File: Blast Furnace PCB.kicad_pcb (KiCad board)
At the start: 2 copper layers, 84 x 60 mm, 35 parts, among them J1 Thermocouple_Screw_Terminal_0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, J2 9V_Conn_01x02, J3 Conn_02x06_Odd_Even, Q1 BSS138, Q2 BSS138, SW1 POWER_SWITCH, U1 MAX31856, U2 I2C_16x2_LCD

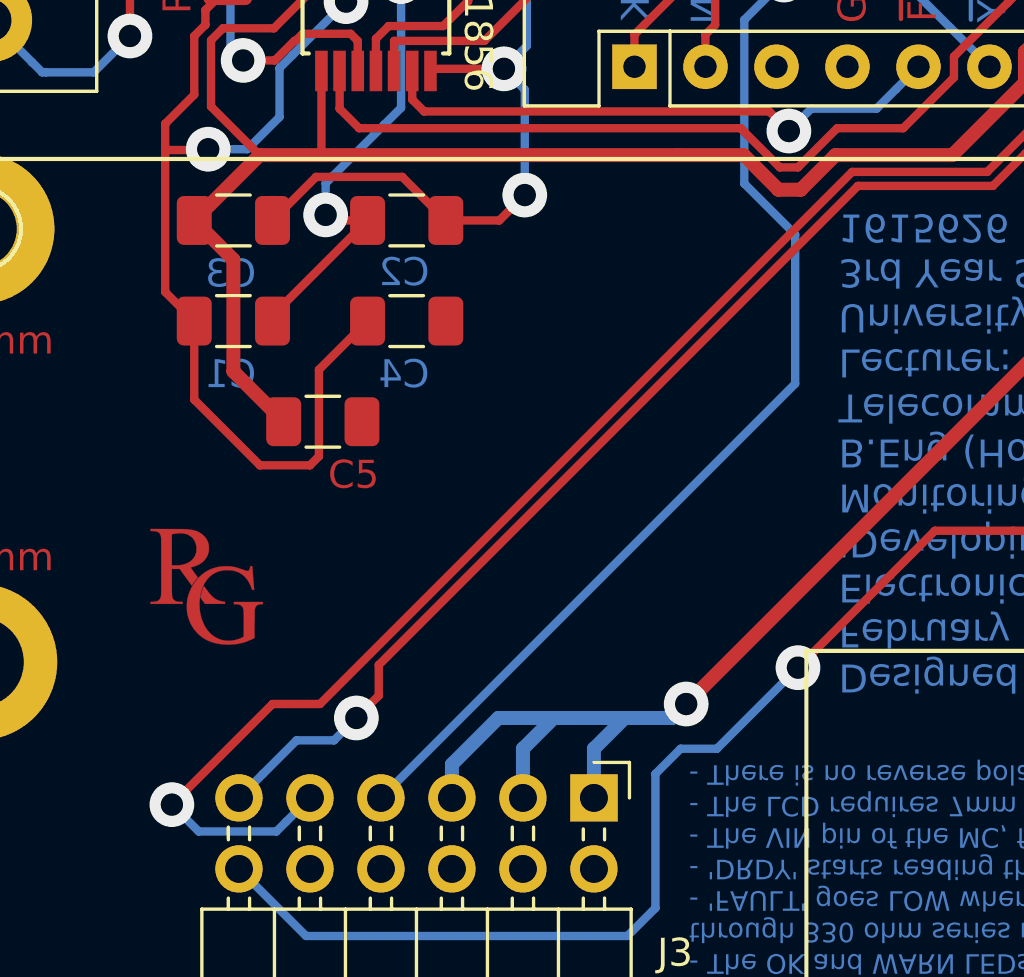
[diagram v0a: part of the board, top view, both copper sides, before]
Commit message: added silly test track
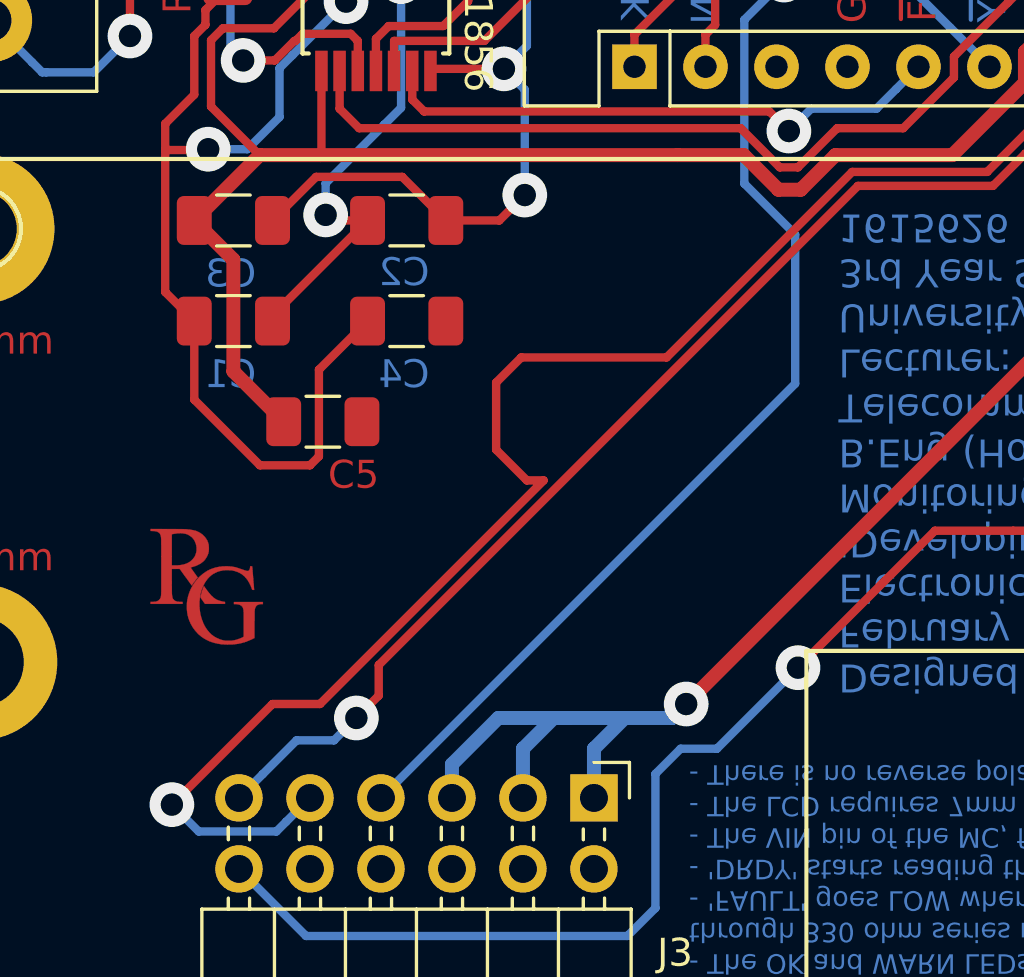
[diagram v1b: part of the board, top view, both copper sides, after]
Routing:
- net /D6: track 61.1 -> 65.9 mm
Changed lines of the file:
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@@
     (thickness 1.6)
     (drawings 81)
-    (tracks 426)
+    (tracks 431)
     (zones 0)
     (modules 35)
@@
   (segment (start 121.150001 111.649999) (end 122.151371 111.649999) (width 0.3) (layer B.Cu) (net 25))
   (segment (start 120.3 112.5) (end 121.150001 111.649999) (width 0.3) (layer B.Cu) (net 25))
-  (segment (start 122.050001 110.952001) (end 120.502002 112.5) (width 0.3) (layer F.Cu) (net 25))
-  (segment (start 122.050001 109.847999) (end 122.050001 110.952001) (width 0.3) (layer F.Cu) (net 25))
-  (segment (start 121.452001 109.249999) (end 122.050001 109.847999) (width 0.3) (layer F.Cu) (net 25))
-  (segment (start 119.482881 109.249999) (end 121.452001 109.249999) (width 0.3) (layer F.Cu) (net 25))
-  (segment (start 117.67067 111.06221) (end 119.482881 109.249999) (width 0.3) (layer F.Cu) (net 25))
-  (segment (start 120.502002 112.5) (end 120.3 112.5) (width 0.3) (layer F.Cu) (net 25))
-  (segment (start 112.83779 111.06221) (end 117.67067 111.06221) (width 0.3) (layer F.Cu) (net 25))
-  (segment (start 93.8 130.1) (end 112.83779 111.06221) (width 0.3) (layer F.Cu) (net 25))
-  (segment (start 93.2 130.1) (end 93.8 130.1) (width 0.3) (layer F.Cu) (net 25))
   (via (at 88.5 133.7) (size 1.6) (drill 0.8) (layers F.Cu B.Cu) (net 25))
-  (segment (start 93.2 130.1) (end 92.1 130.1) (width 0.3) (layer F.Cu) (net 25))
-  (segment (start 92.1 130.1) (end 88.5 133.7) (width 0.3) (layer F.Cu) (net 25))
   (segment (start 92.590001 134.309999) (end 93.44 133.46) (width 0.3) (layer B.Cu) (net 25))
   (segment (start 92.239999 134.660001) (end 92.590001 134.309999) (width 0.3) (layer B.Cu) (net 25))
@@
   (segment (start 88.5 133.7) (end 89.460001 134.660001) (width 0.3) (layer B.Cu) (net 25))
   (via (at 120.3 112.5) (size 1.6) (drill 0.8) (layers F.Cu B.Cu) (net 25))
+  (segment (start 122.050001 109.847999) (end 122.050001 110.952001) (width 0.3) (layer F.Cu) (net 25))
+  (segment (start 120.502002 112.5) (end 120.3 112.5) (width 0.3) (layer F.Cu) (net 25))
+  (segment (start 121.452001 109.249999) (end 122.050001 109.847999) (width 0.3) (layer F.Cu) (net 25))
+  (segment (start 119.482881 109.249999) (end 121.452001 109.249999) (width 0.3) (layer F.Cu) (net 25))
+  (segment (start 112.83779 111.06221) (end 117.67067 111.06221) (width 0.3) (layer F.Cu) (net 25))
+  (segment (start 101 117.7) (end 106.2 117.7) (width 0.3) (layer F.Cu) (net 25))
+  (segment (start 122.050001 110.952001) (end 120.502002 112.5) (width 0.3) (layer F.Cu) (net 25))
+  (segment (start 100.1 118.6) (end 101 117.7) (width 0.3) (layer F.Cu) (net 25))
+  (segment (start 106.2 117.7) (end 112.83779 111.06221) (width 0.3) (layer F.Cu) (net 25))
+  (segment (start 88.5 133.7) (end 92.1 130.1) (width 0.3) (layer F.Cu) (net 25))
+  (segment (start 117.67067 111.06221) (end 119.482881 109.249999) (width 0.3) (layer F.Cu) (net 25))
+  (segment (start 92.1 130.1) (end 93.8 130.1) (width 0.3) (layer F.Cu) (net 25))
+  (segment (start 93.8 130.1) (end 101.8 122.1) (width 0.3) (layer F.Cu) (net 25))
+  (segment (start 101.8 122.1) (end 101.2 122.1) (width 0.3) (layer F.Cu) (net 25))
+  (segment (start 101.2 122.1) (end 100.1 121) (width 0.3) (layer F.Cu) (net 25))
+  (segment (start 100.1 121) (end 100.1 118.6) (width 0.3) (layer F.Cu) (net 25))
   (zone (net 1) (net_name GND) (layer F.Cu) (hatch edge 0.508)
     (connect_pads (clearance 0.508))

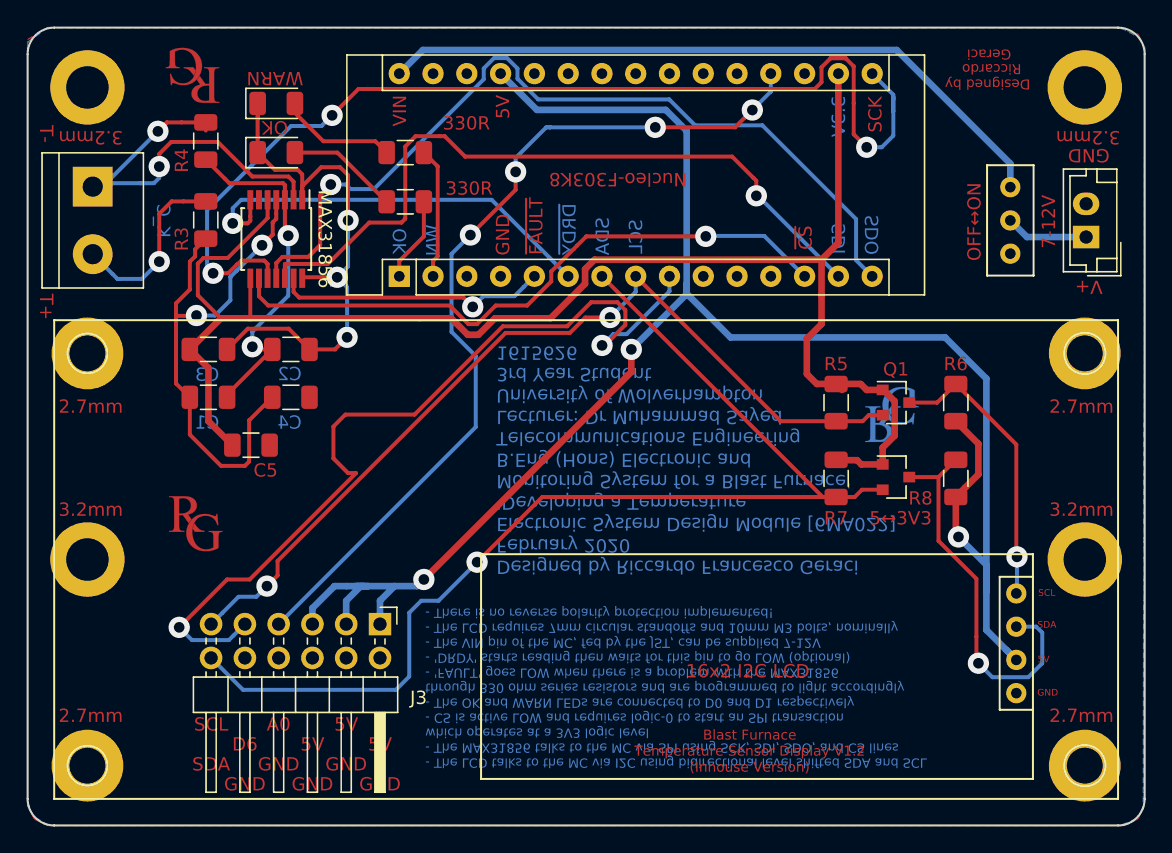
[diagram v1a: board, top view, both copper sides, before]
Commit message: Connected the missed nucleo pads that were meant to be backcopper as chris' email pointed out and made them all on backcopper as they should have been
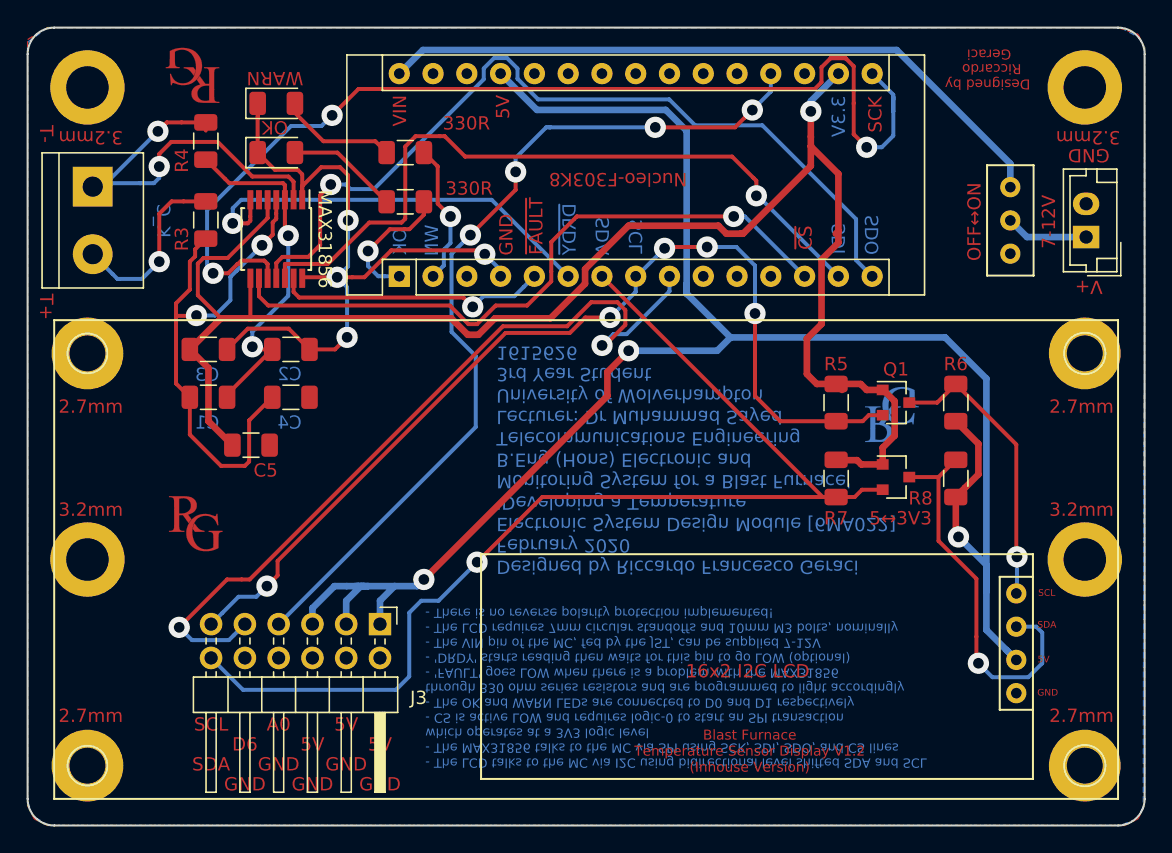
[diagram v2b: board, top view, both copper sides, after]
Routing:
- net GND: track 41.2 -> 55.4 mm, vias 3 -> 4
- net SCL_3V3: track 68.6 -> 76.1 mm, vias 2 -> 5
- net 3V3: track 116.8 -> 122.9 mm, vias 0 -> 1
- net /D6: track 65.9 -> 61.1 mm
- net Net-(A1-Pad1): track 6.37 -> 10.1 mm, vias 0 -> 1
- net /CS: track 47.7 -> 50.2 mm
- net 5V: track 140.7 -> 142.7 mm
- net Net-(A1-Pad2): track 9.87 -> 10.7 mm, vias 0 -> 1

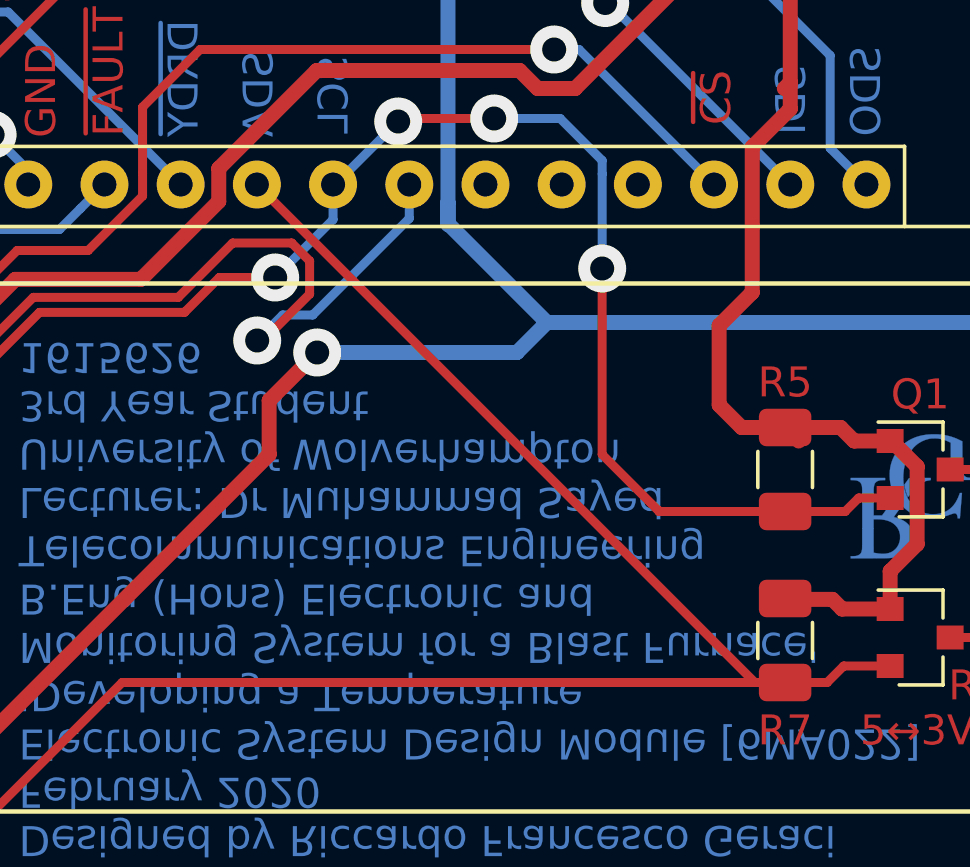
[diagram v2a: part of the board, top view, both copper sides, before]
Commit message: Created gerber files for V1.2.2, and sent to chris
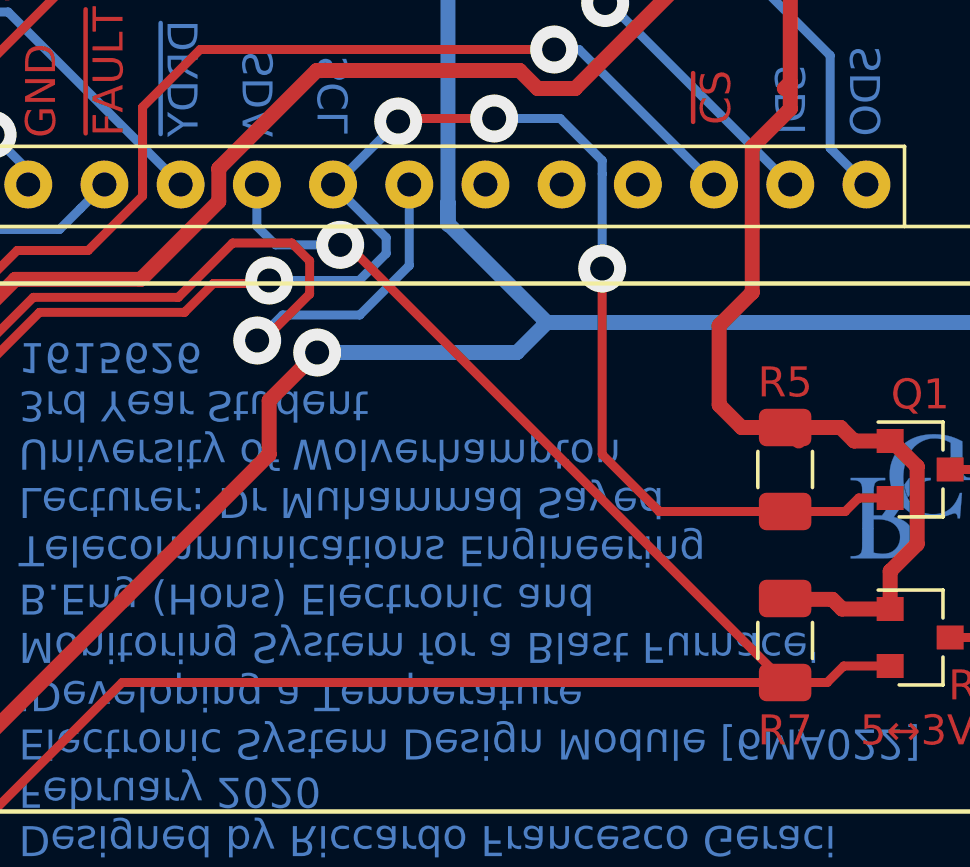
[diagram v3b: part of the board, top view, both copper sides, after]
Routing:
- net SCL_3V3: track 76.1 -> 79.3 mm
- net SDA_3V3: track 85.0 -> 86.8 mm, vias 1 -> 2
- net /D6: track 61.1 -> 62.1 mm
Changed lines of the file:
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@@
     (thickness 1.6)
     (drawings 81)
-    (tracks 469)
+    (tracks 477)
     (zones 0)
     (modules 35)
@@
       (drillshape 0)
       (scaleselection 1)
-      (outputdirectory "Gerber Files/V1.2.1 Chris Version, Back Copper Version/test/"))
+      (outputdirectory "Gerber Files/V1.2.2 Chris Version, ALL back copper!/"))
   )
   (net 0 "")
@@
   (segment (start 126.659999 96.359999) (end 125.09 94.79) (width 0.5) (layer B.Cu) (net 12))
   (segment (start 129.959999 111.9) (end 146.1 111.9) (width 0.5) (layer B.Cu) (net 12))
-  (segment (start 126.659999 108.6) (end 129.959999 111.9) (width 0.5) (layer B.Cu) (net 12))
   (segment (start 126.659999 107.9) (end 126.659999 108.6) (width 0.5) (layer B.Cu) (net 12))
   (segment (start 146.1 111.9) (end 149.2 115) (width 0.5) (layer B.Cu) (net 12))
@@
   (segment (start 128.959999 112.9) (end 129.959999 111.9) (width 0.5) (layer B.Cu) (net 12))
   (segment (start 122.3 112.9) (end 128.959999 112.9) (width 0.5) (layer B.Cu) (net 12))
+  (segment (start 126.659999 108.6) (end 129.959999 111.9) (width 0.5) (layer B.Cu) (net 12))
   (segment (start 93.85 103.12637) (end 93.85 102.81) (width 0.3) (layer F.Cu) (net 13))
   (segment (start 93.85 102.81) (end 93.85 101.55) (width 0.3) (layer F.Cu) (net 13) (status 20))
@@
   (segment (start 105.8 132.6) (end 106.7 131.7) (width 0.3) (layer B.Cu) (net 20))
   (segment (start 106.7 131.7) (end 108 131.7) (width 0.3) (layer B.Cu) (net 20))
-  (segment (start 136.89 123.9) (end 120.29 107.3) (width 0.3) (layer F.Cu) (net 20) (status 20))
+  (via (at 123.067346 109.311799) (size 1.6) (drill 0.8) (layers F.Cu B.Cu) (net 20))
+  (segment (start 137.9 123.9) (end 123.311799 109.311799) (width 0.3) (layer F.Cu) (net 20))
+  (segment (start 123.311799 109.311799) (end 123.067346 109.311799) (width 0.3) (layer F.Cu) (net 20))
+  (segment (start 120.29 108.69) (end 120.29 107.3) (width 0.3) (layer B.Cu) (net 20))
+  (segment (start 123.067346 109.311799) (end 120.911799 109.311799) (width 0.3) (layer B.Cu) (net 20))
+  (segment (start 120.911799 109.311799) (end 120.29 108.69) (width 0.3) (layer B.Cu) (net 20))
   (segment (start 138.5525 117.75) (end 138.35 117.75) (width 0.3) (layer F.Cu) (net 21) (status 30))
   (segment (start 138.35 117.75) (end 137.9 118.2) (width 0.3) (layer F.Cu) (net 21) (status 30))
@@
   (segment (start 137.9 118.2) (end 133.7 118.2) (width 0.3) (layer F.Cu) (net 21) (status 10))
   (segment (start 133.7 118.2) (end 133.7 118.17) (width 0.3) (layer F.Cu) (net 21))
-  (via (at 120.9 110.4) (size 1.6) (drill 0.8) (layers F.Cu B.Cu) (net 21))
-  (segment (start 122.83 108.47) (end 122.83 107.3) (width 0.3) (layer B.Cu) (net 21) (status 20))
-  (segment (start 120.9 110.4) (end 122.83 108.47) (width 0.3) (layer B.Cu) (net 21))
   (segment (start 90.9 133.46) (end 90.9 133.10712) (width 0.3) (layer F.Cu) (net 21))
   (via (at 95.1 130.6) (size 1.6) (drill 0.8) (layers F.Cu B.Cu) (net 21))
@@
   (segment (start 94.300001 131.399999) (end 92.960001 131.399999) (width 0.3) (layer B.Cu) (net 21))
   (segment (start 95.1 130.6) (end 94.300001 131.399999) (width 0.3) (layer B.Cu) (net 21))
-  (segment (start 119.04 110.4) (end 120.9 110.4) (width 0.3) (layer F.Cu) (net 21))
-  (segment (start 117.87778 111.56222) (end 119.04 110.4) (width 0.3) (layer F.Cu) (net 21))
   (segment (start 113.0449 111.56222) (end 117.87778 111.56222) (width 0.3) (layer F.Cu) (net 21))
   (segment (start 95.899999 128.707121) (end 113.0449 111.56222) (width 0.3) (layer F.Cu) (net 21))
@@
   (segment (start 122.9 107.3) (end 122.83 107.3) (width 0.3) (layer B.Cu) (net 21))
   (segment (start 125 105.2) (end 122.9 107.3) (width 0.3) (layer B.Cu) (net 21))
+  (via (at 120.7 110.5) (size 1.6) (drill 0.8) (layers F.Cu B.Cu) (net 21))
+  (segment (start 120.6 110.6) (end 120.7 110.5) (width 0.3) (layer F.Cu) (net 21))
+  (segment (start 118.84 110.6) (end 120.6 110.6) (width 0.3) (layer F.Cu) (net 21))
+  (segment (start 117.87778 111.56222) (end 118.84 110.6) (width 0.3) (layer F.Cu) (net 21))
+  (segment (start 124.6 109.07) (end 122.83 107.3) (width 0.3) (layer B.Cu) (net 21))
+  (segment (start 124.6 109.6) (end 124.6 109.07) (width 0.3) (layer B.Cu) (net 21))
+  (segment (start 123.7 110.5) (end 124.6 109.6) (width 0.3) (layer B.Cu) (net 21))
+  (segment (start 120.7 110.5) (end 123.7 110.5) (width 0.3) (layer B.Cu) (net 21))
   (segment (start 151.45 119.95) (end 146.9 115.4) (width 0.3) (layer F.Cu) (net 22) (status 20))
   (segment (start 143.4 116.8) (end 145.5 116.8) (width 0.3) (layer F.Cu) (net 22) (status 10))
@@
   (segment (start 110.4 104.2) (end 108.979999 105.620001) (width 0.3) (layer B.Cu) (net 24))
   (segment (start 108.979999 105.620001) (end 108.979999 111.479999) (width 0.3) (layer B.Cu) (net 24))
-  (segment (start 125.37 108.43137) (end 125.37 107.3) (width 0.3) (layer B.Cu) (net 25))
-  (segment (start 122.151371 111.649999) (end 125.37 108.43137) (width 0.3) (layer B.Cu) (net 25))
-  (segment (start 121.150001 111.649999) (end 122.151371 111.649999) (width 0.3) (layer B.Cu) (net 25))
-  (segment (start 120.3 112.5) (end 121.150001 111.649999) (width 0.3) (layer B.Cu) (net 25))
   (segment (start 122.050001 110.952001) (end 120.502002 112.5) (width 0.3) (layer F.Cu) (net 25))
   (segment (start 122.050001 109.847999) (end 122.050001 110.952001) (width 0.3) (layer F.Cu) (net 25))
@@
   (segment (start 88.5 133.7) (end 89.460001 134.660001) (width 0.3) (layer B.Cu) (net 25))
   (via (at 120.3 112.5) (size 1.6) (drill 0.8) (layers F.Cu B.Cu) (net 25))
+  (segment (start 125.37 110) (end 125.37 107.3) (width 0.3) (layer B.Cu) (net 25))
+  (segment (start 123.720001 111.649999) (end 125.37 110) (width 0.3) (layer B.Cu) (net 25))
+  (segment (start 121.150001 111.649999) (end 123.720001 111.649999) (width 0.3) (layer B.Cu) (net 25))
+  (segment (start 120.3 112.5) (end 121.150001 111.649999) (width 0.3) (layer B.Cu) (net 25))
   (zone (net 1) (net_name GND) (layer F.Cu) (hatch edge 0.508)
     (connect_pads (clearance 0.508))
